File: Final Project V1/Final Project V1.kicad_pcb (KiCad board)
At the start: 2 copper layers, 30 parts, among them J1 39299043, Q1 SS8050-G, Q2 SS8050-G, SW1 SW_Push, SW2 SW_Push, U1 AP2112K-3.3, U2 ESP32-S3-WROOM-1, U3 BQ21040DBVR

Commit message: Finish V1 Board
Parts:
- added J2: Conn_01x05_Pin, Connector_PinSocket_2.54mm:PinSocket_1x05_P2.54mm_Vertical, F.Cu at (200.0, 132.2)
- added J3: Conn_01x03_Pin, Connector_PinSocket_2.54mm:PinSocket_1x03_P2.54mm_Vertical, F.Cu at (192.6, 123.1)
- added J4: Conn_01x02_Pin, Connector_PinSocket_2.54mm:PinSocket_1x02_P2.54mm_Vertical, F.Cu at (192.6, 132.4)
- added J5: Conn_01x02_Pin, Connector_PinSocket_2.54mm:PinSocket_1x02_P2.54mm_Vertical, F.Cu at (186.0, 128.8)
- added J6: Conn_02x09_Counter_Clockwise, Connector_PinSocket_2.54mm:PinSocket_2x09_P2.54mm_Vertical, F.Cu at (176.4, 98.9)
- added R4: 1k, Resistor_SMD:R_0805_2012Metric_Pad1.20x1.40mm_HandSolder, F.Cu at (189.4, 118.8)
- added R5: 10k, Resistor_SMD:R_0805_2012Metric_Pad1.20x1.40mm_HandSolder, F.Cu at (181.4, 129.6)
- added R7: 10k, Resistor_SMD:R_0805_2012Metric_Pad1.20x1.40mm_HandSolder, F.Cu at (169.6, 109.0)
- added R8: 10k, Resistor_SMD:R_0805_2012Metric_Pad1.20x1.40mm_HandSolder, F.Cu at (177.2, 123.4)
- added R9: 10k, Resistor_SMD:R_0805_2012Metric_Pad1.20x1.40mm_HandSolder, F.Cu at (173.2, 94.8)
- added SW3: SW_Push, Button_Switch_SMD:SW_SPST_B3S-1000, F.Cu at (186.2, 112.4)
- added SW4: SW_Wuerth_450301014042, Button_Switch_THT:SW_Slide-03_Wuerth-WS-SLTV_10x2.5x6.4_P2.54mm, F.Cu at (189.9, 72.6)
- added SW5: SW_Wuerth_450301014042, Button_Switch_THT:SW_Slide-03_Wuerth-WS-SLTV_10x2.5x6.4_P2.54mm, F.Cu at (211.3, 72.6)
- added U4: 2SJ652-1E, 2SJ652-1E:TO-220F-3SG_15P87X10P16_ONS, F.Cu at (168.6, 118.9)
- added U5: 2SJ652-1E, 2SJ652-1E:TO-220F-3SG_15P87X10P16_ONS, F.Cu at (187.4, 123.2)
- R1, R10, R11, R12, R13, R14, R15, R2, R3, R6: footprint Resistor_SMD:R_1206_3216Metric_Pad1.30x1.75mm_HandSolder -> Resistor_SMD:R_0805_2012Metric_Pad1.20x1.40mm_HandSolder
- moved R15 121.3 mm to (191.6, 94.8)
- moved D2 101.7 mm to (209.0, 91.5), turned to 90 degrees
- moved SW1 90.5 mm to (183.8, 92.8)
- moved R14 74.8 mm to (204.0, 95.0)
- moved C10 73.6 mm to (210.8, 95.8), turned to -90 degrees
- moved SW2 70.5 mm to (206.4, 125.0)
- moved C5 66.5 mm to (208.2, 95.8), turned to -90 degrees
- moved R11 61.8 mm to (195.6, 96.2), turned to -90 degrees
- moved USB-C1 61.6 mm to (200.5, 77.6), turned to 180 degrees
- moved C4 61.3 mm to (198.4, 85.8)
- moved R1 60.0 mm to (193.8, 80.2)
- moved R12 59.5 mm to (191.6, 97.4)
- moved Q1 58.2 mm to (199.1, 95.4)
- moved C2 58.1 mm to (201.2, 90.6), turned to 90 degrees
- moved R10 57.4 mm to (199.4, 124.5), turned to 90 degrees
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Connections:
- J1 pad 1: Net-(D2-A) -> Net-(SW5-C)
- U2 pad 10: unconnected-(U2-IO17-Pad10) -> D1
- U2 pad 11: unconnected-(U2-IO18-Pad11) -> D0
- U2 pad 17: unconnected-(U2-IO9-Pad17) -> VS
- U2 pad 18: unconnected-(U2-IO10-Pad18) -> HS
- U2 pad 19: unconnected-(U2-IO11-Pad19) -> PCLK
- U2 pad 20: unconnected-(U2-IO12-Pad20) -> MCLK
- U2 pad 21: unconnected-(U2-IO13-Pad21) -> D7
- U2 pad 22: unconnected-(U2-IO14-Pad22) -> D6
- U2 pad 23: unconnected-(U2-IO21-Pad23) -> D5
- U2 pad 24: unconnected-(U2-IO47-Pad24) -> D4
- U2 pad 25: unconnected-(U2-IO48-Pad25) -> Camera Power Signal
- U2 pad 26: unconnected-(U2-IO45-Pad26) -> Motor Power Signal
- U2 pad 32: unconnected-(U2-IO39-Pad32) -> Hall Read
- U2 pad 33: unconnected-(U2-IO40-Pad33) -> Manual Feed
- U2 pad 36: unconnected-(U2-RXD0-Pad36) -> RX
- U2 pad 37: unconnected-(U2-TXD0-Pad37) -> TX
- U2 pad 38: unconnected-(U2-IO2-Pad38) -> SDA
- U2 pad 39: unconnected-(U2-IO1-Pad39) -> SCL
- U2 pad 7: unconnected-(U2-IO7-Pad7) -> Microcontroller Charge Read
- U2 pad 8: unconnected-(U2-IO15-Pad8) -> D3
- U2 pad 9: unconnected-(U2-IO16-Pad9) -> D2
- USB-C1 pad A9: Net-(D1-A) -> Net-(SW4-B)
- USB-C1 pad B9: Net-(D1-A) -> Net-(SW4-B)
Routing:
- net Net-(U2-IO0): track 0.00 -> 101.6 mm, vias 0 -> 4
- net SCL: track 0.00 -> 94.9 mm, vias 0 -> 2
- net SDA: track 0.00 -> 60.4 mm, vias 0 -> 2
- net D2: track 0.00 -> 55.2 mm, vias 0 -> 1
- net Camera Power: track 0.00 -> 51.8 mm, vias 0 -> 1
- net GND: track 0.00 -> 51.5 mm, vias 0 -> 28
- net DTR: track 0.00 -> 50.1 mm, vias 0 -> 1
- net 3.3V: track 0.00 -> 46.3 mm, vias 0 -> 11
- net RTS: track 0.00 -> 45.3 mm, vias 0 -> 1
- net D3: track 0.00 -> 41.4 mm
- net Chip_PU: track 0.00 -> 41.2 mm, vias 0 -> 2
- net D0: track 0.00 -> 39.4 mm, vias 0 -> 2
- net D1: track 0.00 -> 35.3 mm, vias 0 -> 1
- net HS: track 0.00 -> 31.5 mm, vias 0 -> 1
- net Camera Power Signal: track 0.00 -> 30.1 mm, vias 0 -> 1
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- added copper zone on F.Cu, net 3.3V
- added copper zone on B.Cu, net GND
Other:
- board outline added: 67.4 x 68 mm
- board text added: "SAFF Main Board V1.0"

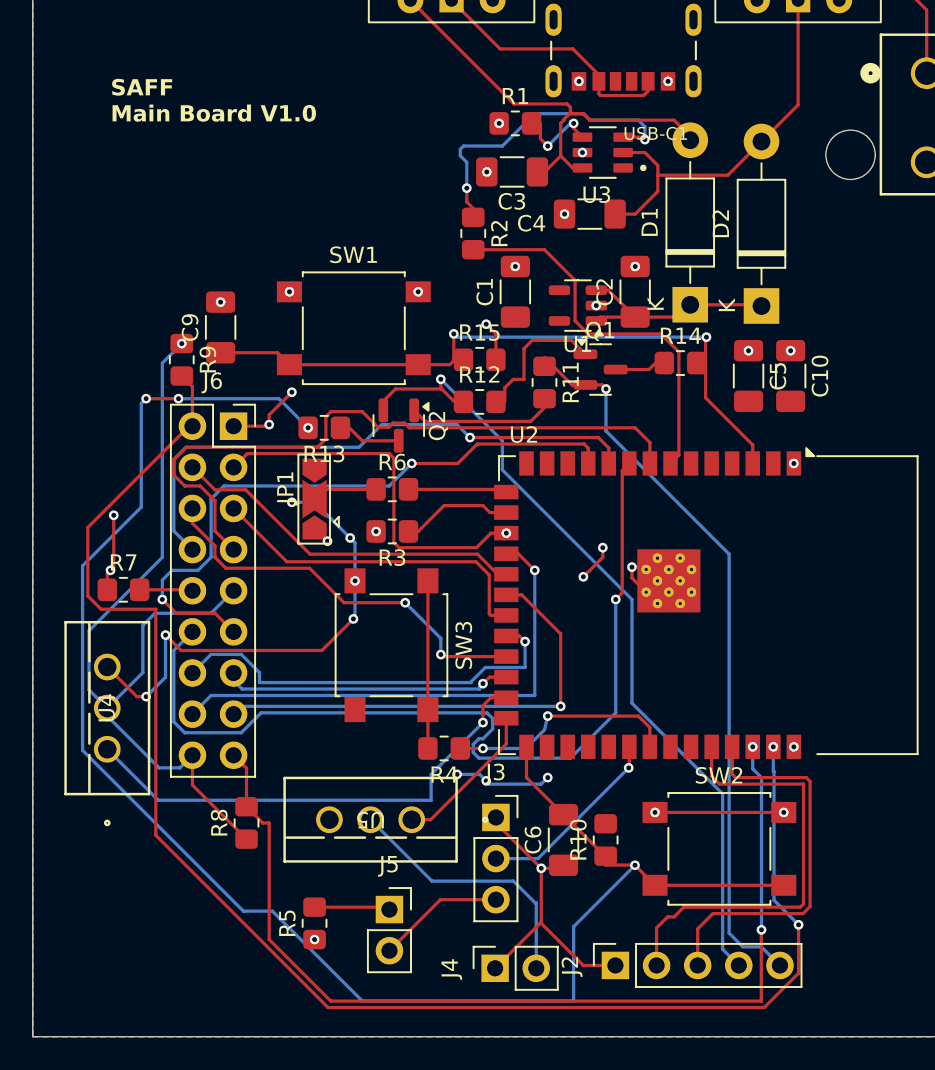
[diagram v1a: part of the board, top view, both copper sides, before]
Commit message: Change socket headers to pins and use through-hole buttons. Need to try switch on pcb when arrives and change camera connector
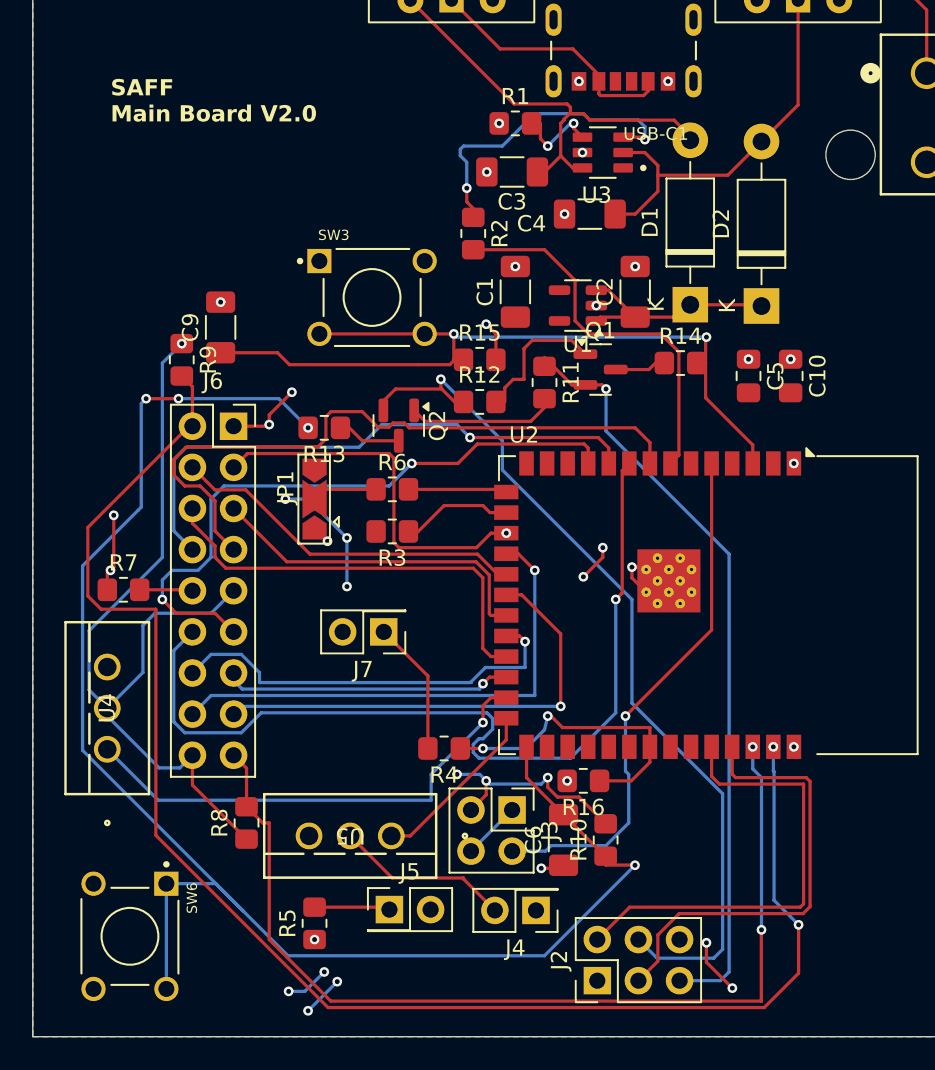
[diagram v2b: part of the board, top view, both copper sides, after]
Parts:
- removed SW1, SW2: SW_Push, Button_Switch_SMD:SW_SPST_B3S-1000
- added J7: Conn_02x01, Connector_PinHeader_2.54mm:PinHeader_2x01_P2.54mm_Vertical, F.Cu at (185.7, 111.6)
- added R16: 10k, Resistor_SMD:R_0805_2012Metric_Pad1.20x1.40mm_HandSolder, F.Cu at (198.0, 120.8)
- added SW6: 1825910-6, 1825910_6:SW_1825910-6-4, F.Cu at (170.0, 130.4)
- C10: value 10uF (1206) -> 10uF (0805); footprint Capacitor_SMD:C_1206_3216Metric_Pad1.33x1.80mm_HandSolder -> Capacitor_SMD:C_0805_2012Metric_Pad1.18x1.45mm_HandSolder
- C5: value 100nF (1206) -> .1uF (0805); footprint Capacitor_SMD:C_1206_3216Metric_Pad1.33x1.80mm_HandSolder -> Capacitor_SMD:C_0805_2012Metric_Pad1.18x1.45mm_HandSolder
- J2: value Conn_01x05_Pin -> Conn_02x03_Counter_Clockwise; footprint Connector_PinSocket_2.54mm:PinSocket_1x05_P2.54mm_Vertical -> Connector_PinHeader_2.54mm:PinHeader_2x03_P2.54mm_Vertical
- J3: value Conn_01x03_Pin -> Conn_02x02_Counter_Clockwise; footprint Connector_PinSocket_2.54mm:PinSocket_1x03_P2.54mm_Vertical -> Connector_PinHeader_2.54mm:PinHeader_2x02_P2.54mm_Vertical
- J4, J5: value Conn_01x02_Pin -> Conn_02x01; footprint Connector_PinSocket_2.54mm:PinSocket_1x02_P2.54mm_Vertical -> Connector_PinHeader_2.54mm:PinHeader_2x01_P2.54mm_Vertical
- R5: value 10k -> 1k
- SW3: value SW_Push -> 1825910-6; footprint Button_Switch_SMD:SW_SPST_B3S-1000 -> 1825910_6:SW_1825910-6-4
- moved SW3 21.5 mm to (184.9, 91.0), turned to 0 degrees
- moved J4 4.38 mm to (195.1, 128.8), turned to 180 degrees
- moved U5 1.61 mm to (186.1, 124.2)
- moved J2 1.46 mm to (198.9, 133.1)
- moved J3 1.10 mm to (193.6, 122.6), turned to -90 degrees
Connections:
- R4 pad 2: Net-(R4-Pad2) -> Net-(J7-Pin_1)
- SW3 pad 1: Net-(R4-Pad2) -> GND
- SW3 pad 2: 3.3V -> GND
- U2 pad 32: Hall Read -> unconnected-(U2-IO39-Pad32)
- U2 pad 5: unconnected-(U2-IO5-Pad5) -> Hall Read
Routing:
- net Hall Read: track 11.8 -> 32.4 mm
- net GND: track 51.5 -> 33.2 mm, vias 28 -> 27
- net 3.3V: track 46.3 -> 28.8 mm
- net Net-(R4-Pad2): track 10.3 -> 0.00 mm
- net Net-(J7-Pin_1): track 0.00 -> 8.33 mm
- net Chip_PU: track 41.2 -> 49.5 mm
- net Motor Out: track 16.4 -> 10.9 mm
- net Manual Feed: track 14.5 -> 19.1 mm
- net DTR: track 50.1 -> 54.5 mm
- net TX: track 24.2 -> 27.9 mm
- net Net-(U2-IO0): track 101.6 -> 98.9 mm
- net D5: track 24.7 -> 26.7 mm, vias 2 -> 0
- net RTS: track 45.3 -> 47.0 mm
- net RX: track 27.1 -> 28.8 mm
- net Motor Power Signal: track 9.37 -> 10.9 mm
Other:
- board text added: "SAFF Main Board V2.0"
- board text removed: "SAFF Main Board V1.0"

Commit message: V2 Board
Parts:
- removed J6: Conn_02x09_Counter_Clockwise, Connector_PinSocket_2.54mm:PinSocket_2x09_P2.54mm_Vertical
- added H1: MountingHoleM3, MountingHole:MountingHole_3.2mm_M3_DIN965, F.Cu at (227.0, 72.2)
- added H2: MountingHoleM3, MountingHole:MountingHole_3.2mm_M3_DIN965, F.Cu at (226.0, 137.0)
- added H3: MountingHoleM3, MountingHole:MountingHole_3.2mm_M3_DIN965, F.Cu at (150.8, 135.6)
- added H4: MountingHoleM3, MountingHole:MountingHole_3.2mm_M3_DIN965, F.Cu at (161.4, 104.6)
- added J8: 75867-132LF, 75867_132LF:HDRRA8W62P254_4X2_1737X957H920, F.Cu at (174.0, 81.6)
- added J9: 10056845-110LF, 75867-101LF:CON10_2X5_R2_FCI_GLE, F.Cu at (150.9, 81.6)
- moved U4 27.7 mm to (165.0, 91.4), turned to -90 degrees
- moved R7 24.3 mm to (163.8, 85.4), turned to 90 degrees
- moved R9 11.1 mm to (166.4, 86.0), turned to 90 degrees
- moved J7 7.42 mm to (185.1, 119.0)
- moved C9 7.07 mm to (182.0, 95.8), turned to 180 degrees
- moved JP1 3.01 mm to (178.4, 103.6)
- moved USB-C1 2.30 mm to (200.4, 75.3)
- moved J1 1.10 mm to (219.2, 78.2)
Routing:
- net D7: track 21.0 -> 76.2 mm
- net D4: track 17.9 -> 72.9 mm, vias 1 -> 0
- net PCLK: track 22.1 -> 76.8 mm
- net VS: track 23.0 -> 77.5 mm, vias 1 -> 0
- net SDA: track 60.4 -> 114.7 mm, vias 2 -> 1
- net D5: track 26.7 -> 76.1 mm
- net D6: track 25.4 -> 73.1 mm, vias 1 -> 0
- net D0: track 39.4 -> 84.6 mm
- net MCLK: track 29.2 -> 73.2 mm, vias 1 -> 0
- net HS: track 31.5 -> 73.5 mm, vias 1 -> 0
- net Camera Power Signal: track 30.1 -> 65.1 mm
- net D1: track 35.3 -> 64.0 mm, vias 1 -> 2
- net D3: track 41.4 -> 68.2 mm, vias 0 -> 2
- net SCL: track 94.9 -> 118.6 mm
- net Net-(J8-Pad7): track 3.28 -> 21.7 mm, vias 0 -> 1
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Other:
- board size 67.4 x 68 mm -> 85.6 x 72 mm

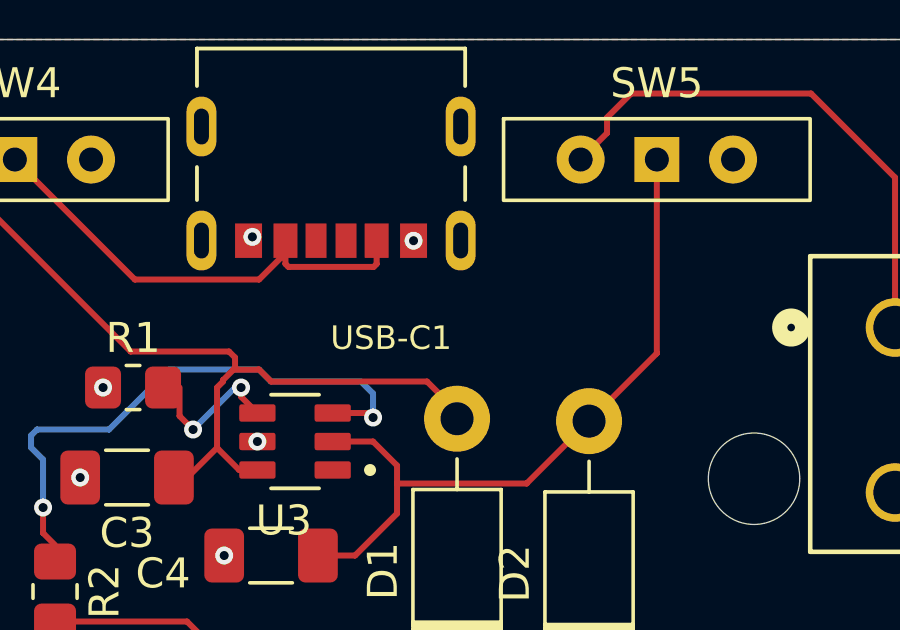
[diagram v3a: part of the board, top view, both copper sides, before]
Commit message: Added resistors to control channel on USB-C cause I am a silly goose and didn't do that before
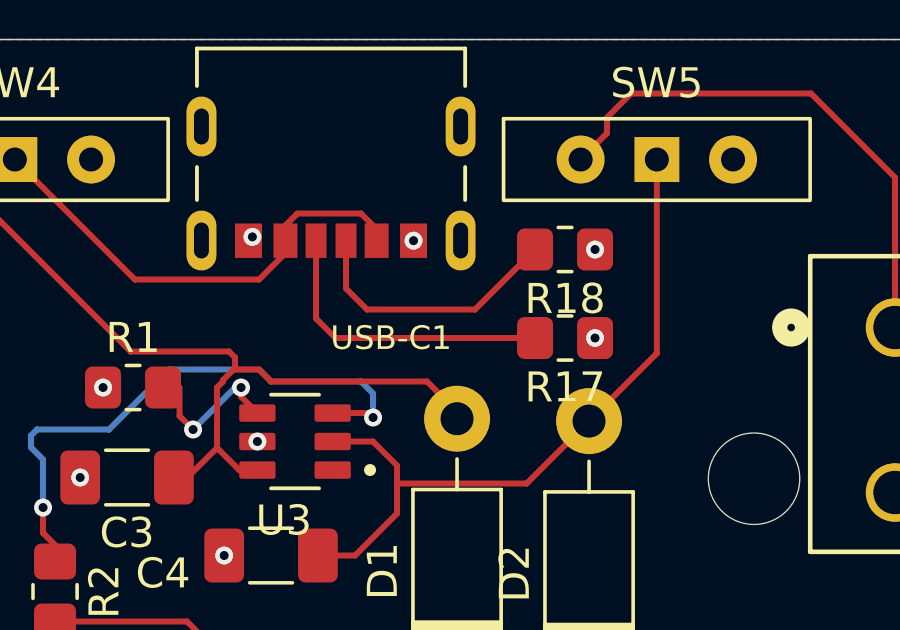
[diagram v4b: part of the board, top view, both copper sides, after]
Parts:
- added R17: 5.1k, Resistor_SMD:R_0805_2012Metric_Pad1.20x1.40mm_HandSolder, F.Cu at (208.2, 78.5)
- added R18: 5.1k, Resistor_SMD:R_0805_2012Metric_Pad1.20x1.40mm_HandSolder, F.Cu at (208.2, 75.6)
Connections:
- USB-C1 pad A5: unconnected-(USB-C1-CC1-PadA5) -> Net-(USB-C1-CC1)
- USB-C1 pad B5: unconnected-(USB-C1-CC2-PadB5) -> Net-(USB-C1-CC2)
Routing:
- net Net-(USB-C1-CC2): track 0.00 -> 10.2 mm
- net Net-(USB-C1-CC1): track 0.00 -> 9.01 mm
- net GND: vias 28 -> 30

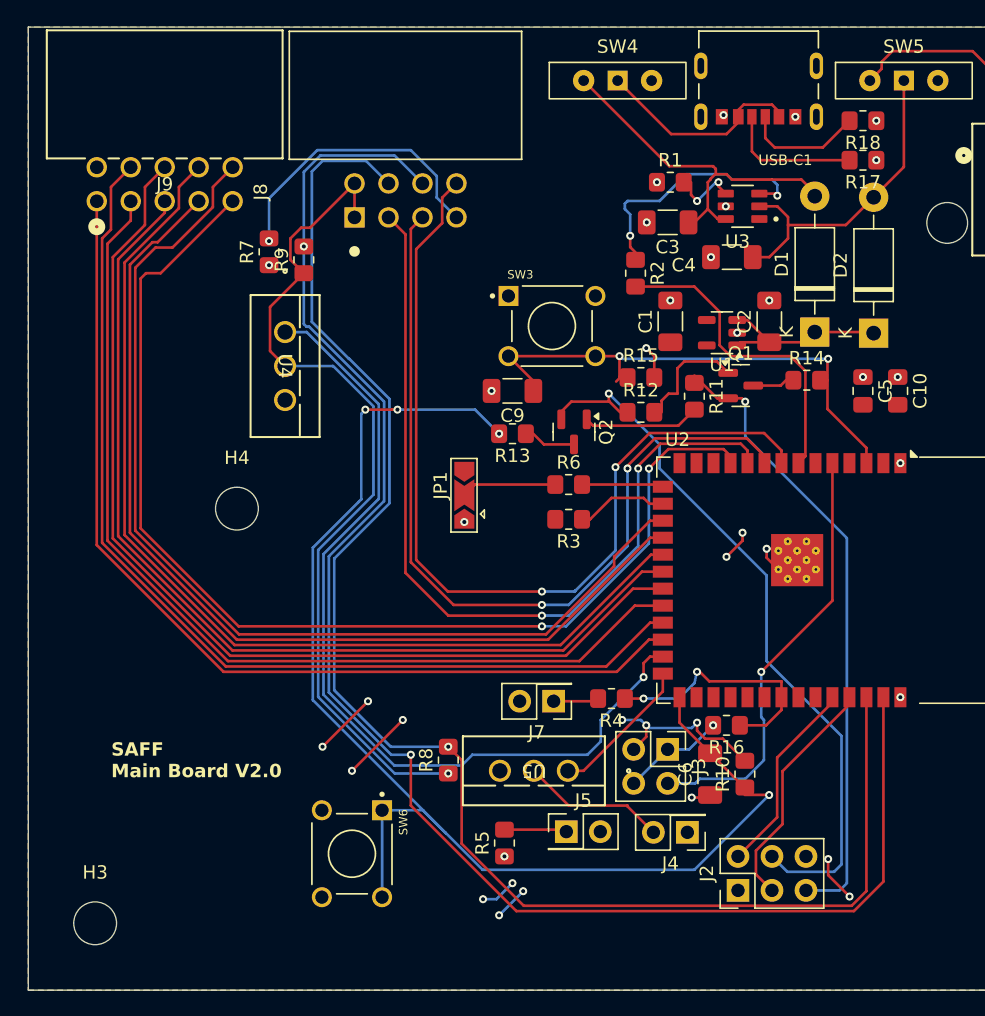
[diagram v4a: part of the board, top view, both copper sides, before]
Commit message: V4 Schematic. Will work with V3
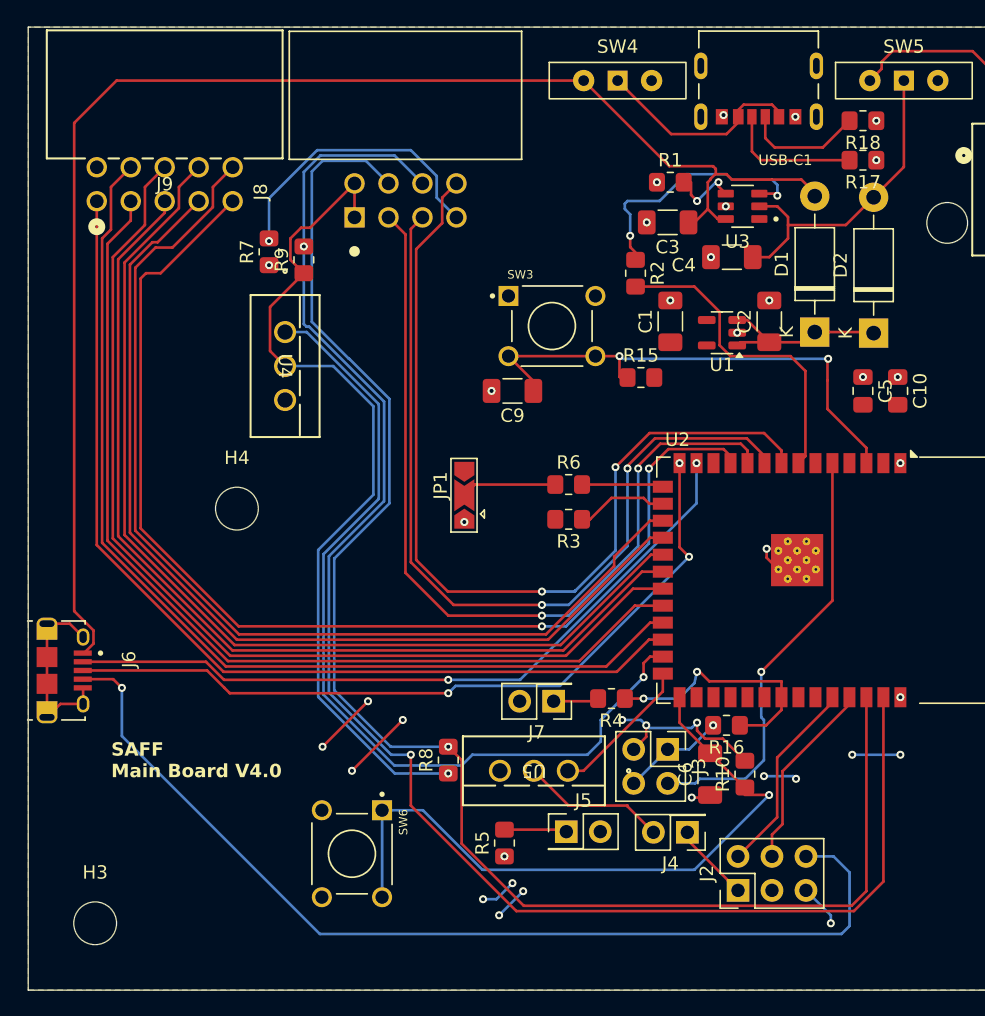
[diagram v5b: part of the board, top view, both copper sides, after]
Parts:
- removed Q1, Q2: SS8050-G, Package_TO_SOT_SMD:SOT-23
- removed R11, R12, R13, R14: 10k, Resistor_SMD:R_0805_2012Metric_Pad1.20x1.40mm_HandSolder
- added J6: 10118194-0001LF, 10118194_0001LF:AMPHENOL_10118194-0001LF, F.Cu at (147.2, 116.7)
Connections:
- net Net-(D1-A) renamed 5V
- J2 pad 3: TX -> GND
- J2 pad 4: DTR -> TX
- J2 pad 5: RTS -> 3.3V
- J2 pad 6: GND -> ID
- SW4 pad 3: unconnected-(SW4-A-Pad3) -> GND
- SW5 pad 3: unconnected-(SW5-A-Pad3) -> GND
- U2 pad 13: unconnected-(U2-USB_D--Pad13) -> D-
- U2 pad 14: unconnected-(U2-USB_D+-Pad14) -> D+
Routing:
- net 5V: track 27.6 -> 107.7 mm
- net ID: track 0.00 -> 75.3 mm, vias 0 -> 1
- net D+: track 0.00 -> 57.5 mm, vias 0 -> 3
- net D-: track 0.00 -> 54.9 mm, vias 0 -> 2
- net DTR: track 54.5 -> 0.00 mm, vias 1 -> 0
- net Net-(U2-IO0): track 98.9 -> 50.7 mm, vias 4 -> 1
- net RTS: track 47.0 -> 0.00 mm, vias 1 -> 0
- net GND: track 36.9 -> 51.5 mm, vias 30 -> 26
- net Net-(Q2-B): track 8.74 -> 0.00 mm
- net Net-(Q1-B): track 8.53 -> 0.00 mm
- net 3.3V: track 21.0 -> 27.9 mm, vias 8 -> 12
- net TX: track 17.8 -> 14.3 mm
- net Net-(Q2-C): track 3.38 -> 0.00 mm
- net Net-(Q1-C): track 2.62 -> 0.00 mm
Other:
- board text added: "SAFF Main Board V4.0"
- board text removed: "SAFF Main Board V2.0"
